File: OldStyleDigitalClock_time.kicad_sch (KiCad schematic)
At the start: 13 parts, among them U12 CD4060BM, U13 CD4017BM, U14 CD4017BM, U15 CD4017BM, Y1 HC49 XTAL (32768 Hz)

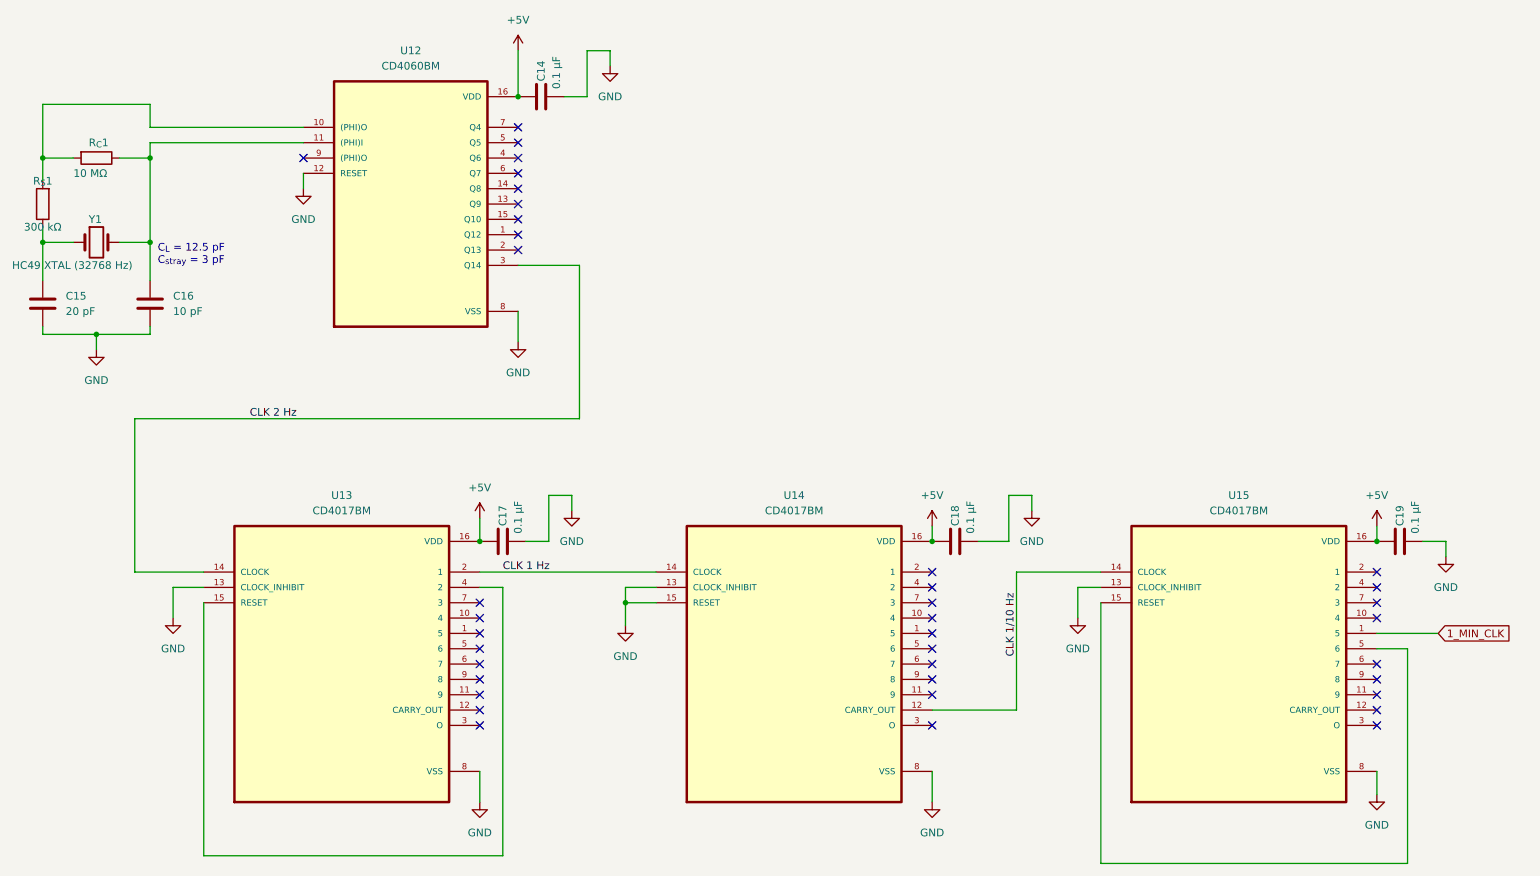
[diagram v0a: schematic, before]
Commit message: Changed units for caps
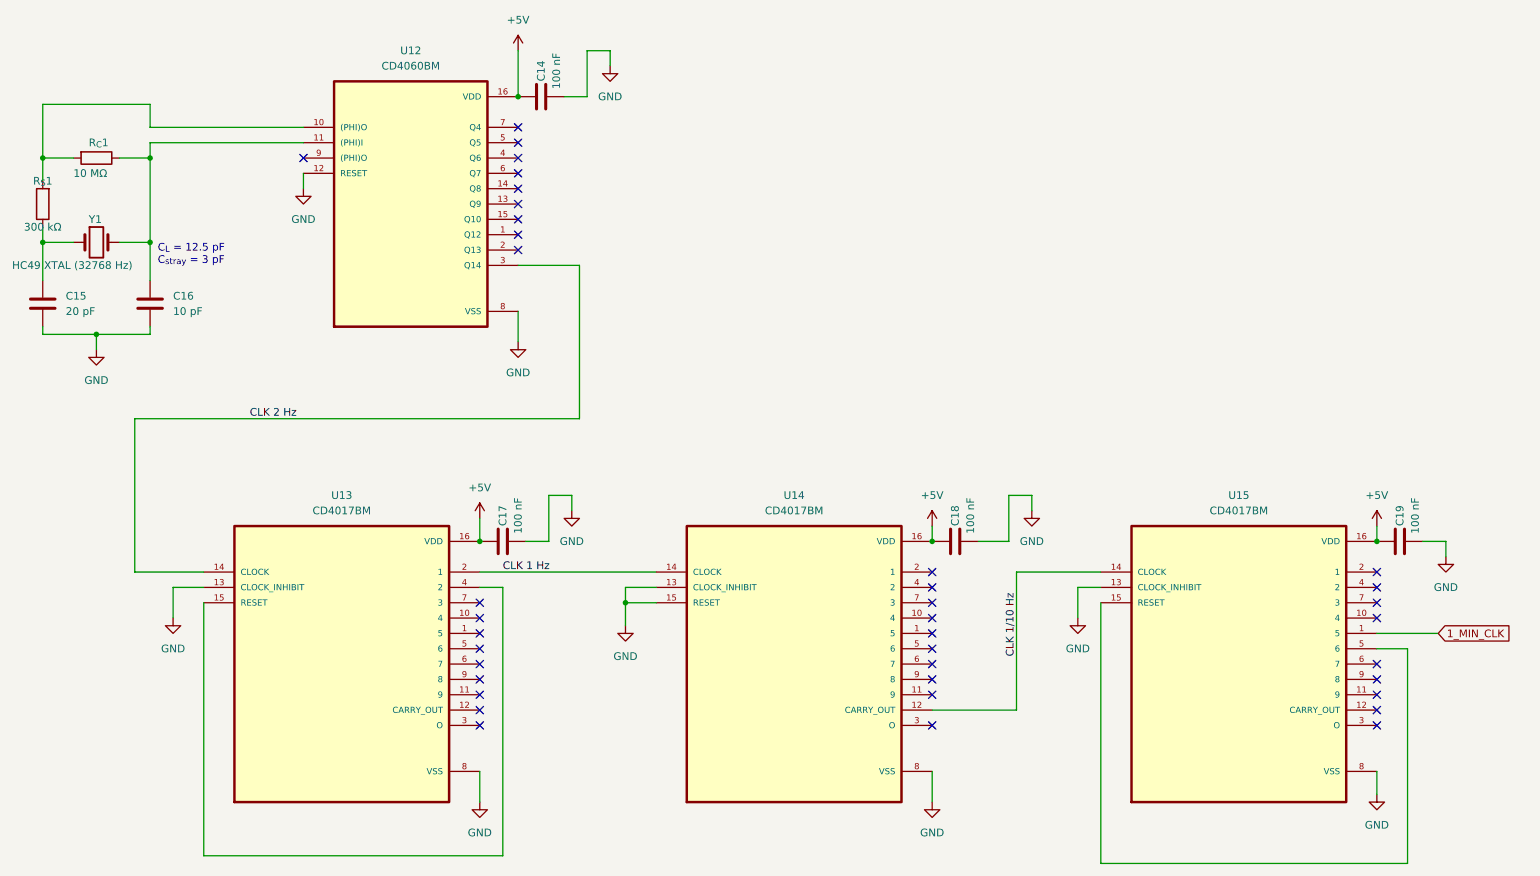
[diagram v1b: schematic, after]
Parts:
- C14, C17, C18, C19: value 0.1 µF -> 100 nF
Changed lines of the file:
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@@
 			)
 		)
-		(property "Value" "0.1 µF"
+		(property "Value" "100 nF"
 			(at 119.38 30.48 0)
 			(effects
@@
 			)
 		)
-		(property "Value" "0.1 µF"
+		(property "Value" "100 nF"
 			(at 187.96 104.14 0)
 			(effects
@@
 			)
 		)
-		(property "Value" "0.1 µF"
+		(property "Value" "100 nF"
 			(at 261.62 104.14 0)
 			(effects
@@
 			)
 		)
-		(property "Value" "0.1 µF"
+		(property "Value" "100 nF"
 			(at 113.03 104.14 0)
 			(effects

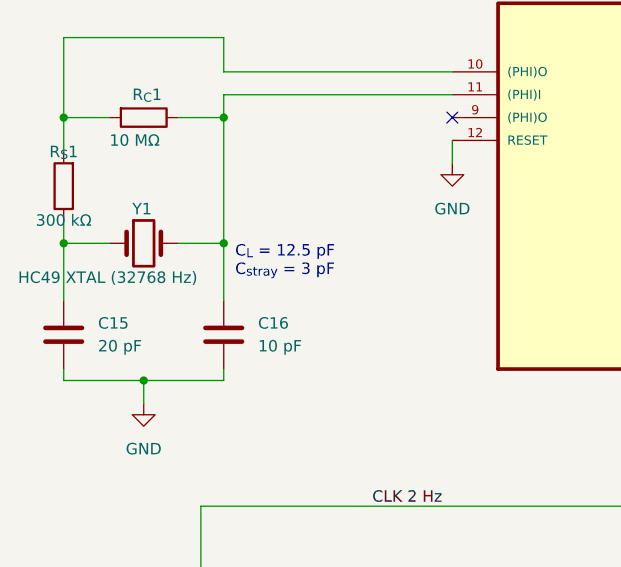
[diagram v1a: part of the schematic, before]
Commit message: Updated Pierce oscillator values with working values on PCB
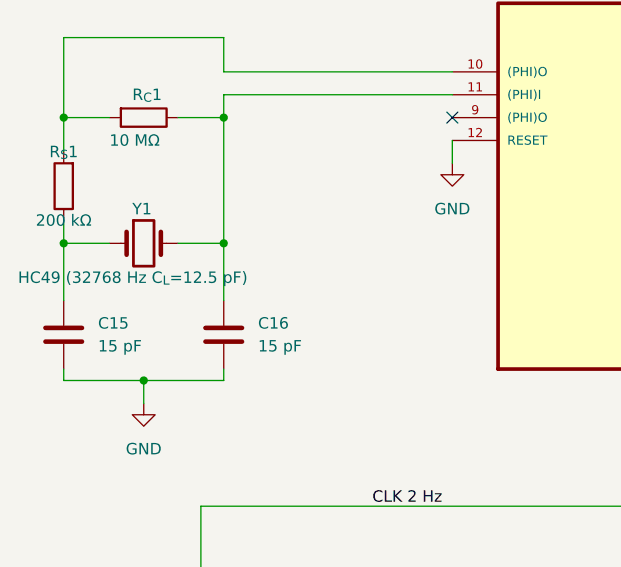
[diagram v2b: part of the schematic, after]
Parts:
- C15: value 20 pF -> 15 pF
- C16: value 10 pF -> 15 pF
- R_{S}1: value 300 kΩ -> 200 kΩ
- Y1: value HC49 XTAL (32768 Hz) -> HC49 (32768 Hz C_{L}=12.5 pF)
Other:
- note removed: "C_{L} = 12.5 pF C_{stray} = 3 pF"
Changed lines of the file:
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@@
 		(company "Pasquale Lafiosca")
-	)
-	(text "C_{L} = 12.5 pF\nC_{stray} = 3 pF"
-		(exclude_from_sim no)
-		(at 53.34 59.69 0)
-		(effects
-			(font
-				(size 1.27 1.27)
-			)
-			(justify left bottom)
-		)
 	)
 	(junction
@@
 			)
 		)
-		(property "Value" "10 pF"
+		(property "Value" "15 pF"
 			(at 55.88 67.3099 0)
 			(effects
@@
 			)
 		)
-		(property "Value" "20 pF"
+		(property "Value" "15 pF"
 			(at 38.1 67.3099 0)
 			(effects
@@
 			)
 		)
-		(property "Value" "HC49 XTAL (32768 Hz)"
+		(property "Value" "HC49 (32768 Hz C_{L}=12.5 pF)"
 			(at 29.21 59.69 0)
 			(effects
@@
 			)
 		)
-		(property "Value" "300 kΩ"
+		(property "Value" "200 kΩ"
 			(at 34.29 53.34 0)
 			(effects

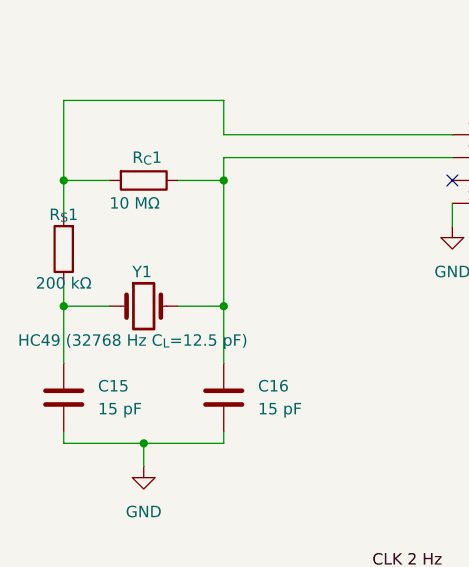
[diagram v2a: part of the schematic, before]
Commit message: Restored old Rs value of 300k
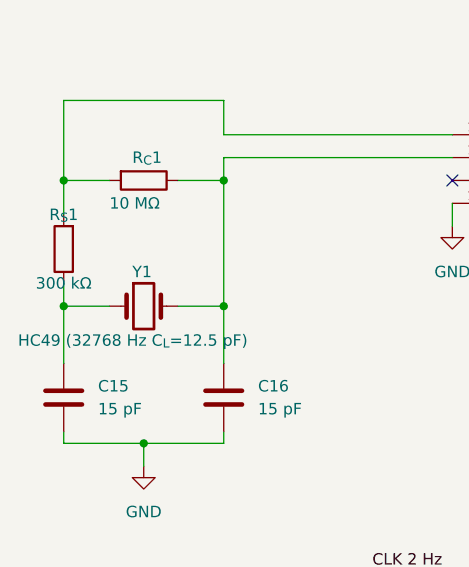
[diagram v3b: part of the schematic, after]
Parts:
- R_{S}1: value 200 kΩ -> 300 kΩ
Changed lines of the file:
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@@
 			)
 		)
-		(property "Value" "200 kΩ"
+		(property "Value" "300 kΩ"
 			(at 34.29 53.34 0)
 			(effects
